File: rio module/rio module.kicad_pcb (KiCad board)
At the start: 2 copper layers, 60 x 45 mm, 11 parts, among them J1 MTJ-88ARX1-FSM-LG, J2 MTJ-88ARX1-FSM-LG, J3 Conn_01x02_Pin, J4 Conn_01x02_Pin, J5 Conn_01x02_Pin, J6 Conn_01x02_Pin, J7 Conn_01x02_Pin, SW1 SW_DPST

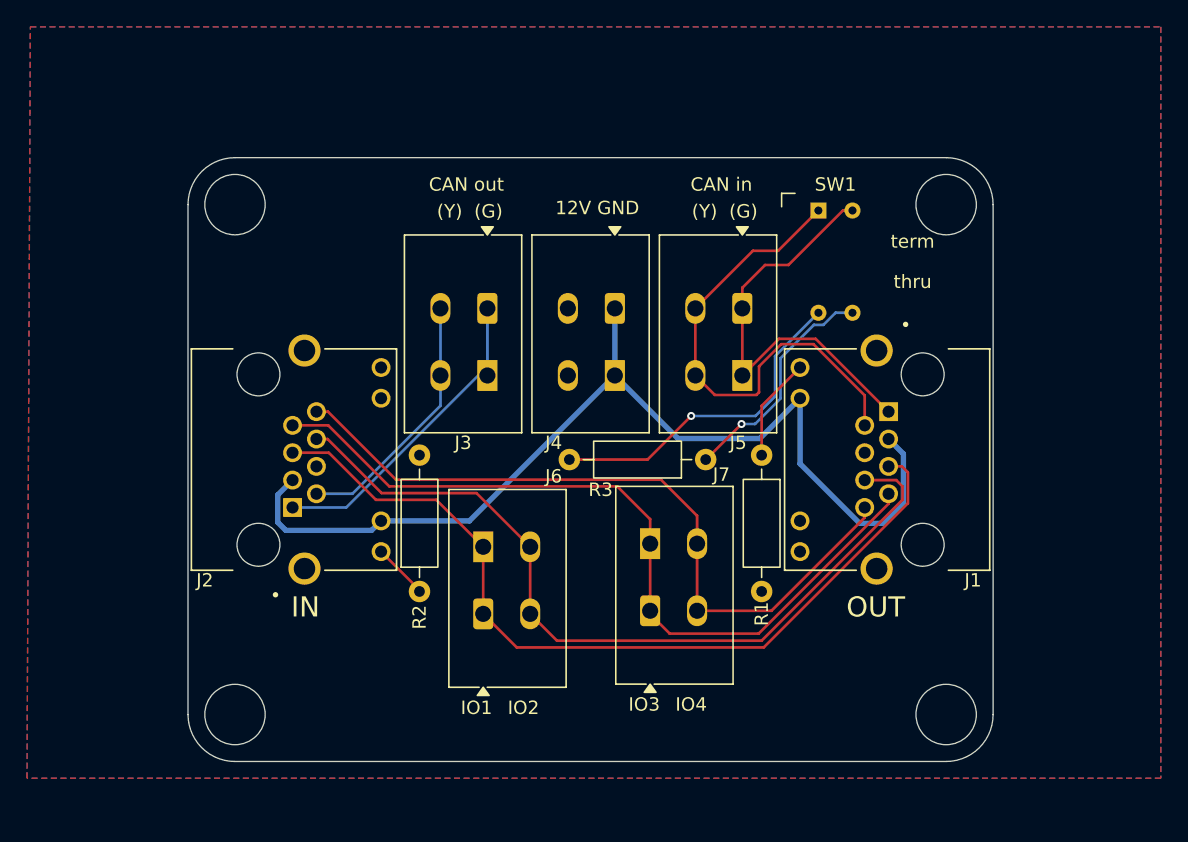
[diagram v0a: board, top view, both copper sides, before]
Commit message: removed mxp crossover, moved to hardwired DIO, switching from DIO WAGOs to Molex SL
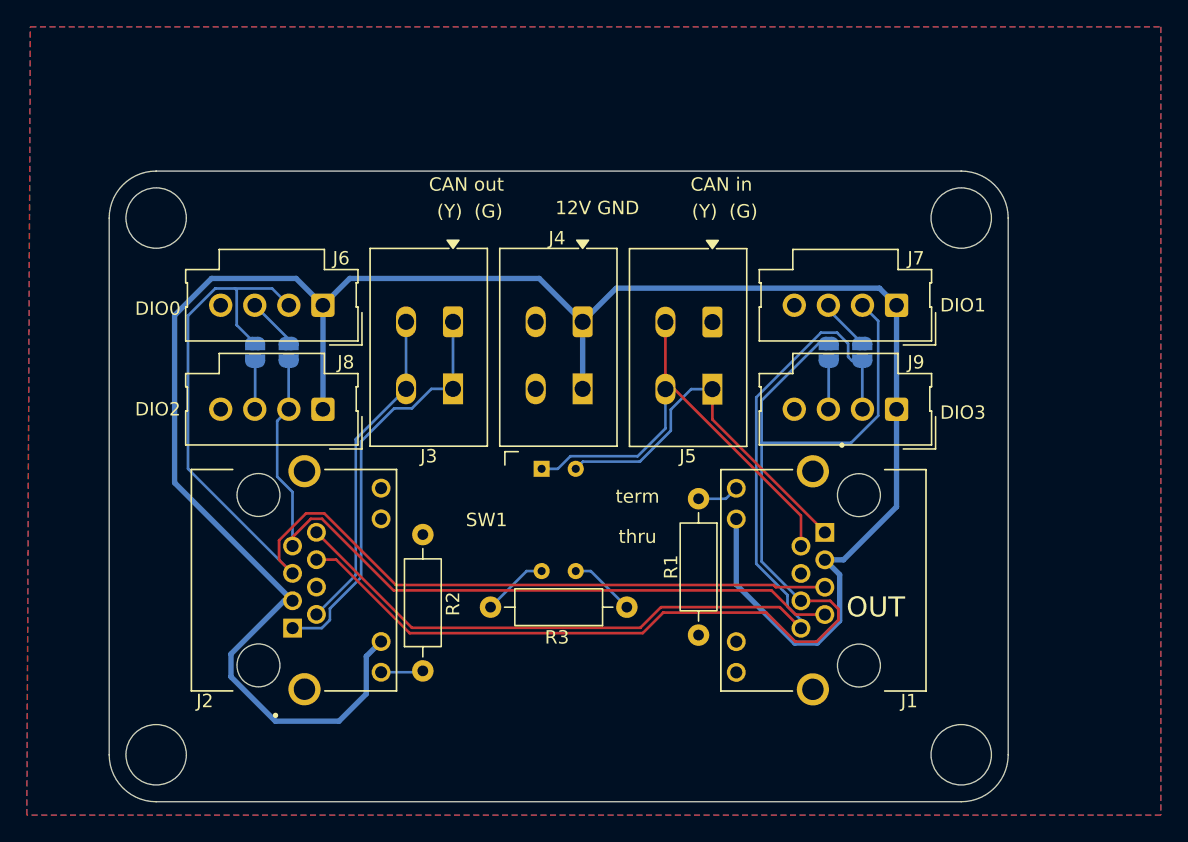
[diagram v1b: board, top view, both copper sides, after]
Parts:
- added J8: Conn_01x04_Pin, custom:Molex_SL_171971-0004_1x04_P2.54mm_Vertical, F.Cu at (55.6, 69.5)
- added J9: Conn_01x04_Pin, custom:Molex_SL_171971-0004_1x04_P2.54mm_Vertical, F.Cu at (98.3, 69.5)
- added REF**: SolderJumper-2_P1.3mm_Open_RoundedPad1.0x1.5mm, Jumper:SolderJumper-2_P1.3mm_Open_RoundedPad1.0x1.5mm, B.Cu at (95.8, 65.2)
- added REF**: SolderJumper-2_P1.3mm_Open_RoundedPad1.0x1.5mm, Jumper:SolderJumper-2_P1.3mm_Open_RoundedPad1.0x1.5mm, B.Cu at (93.2, 65.2)
- added REF**: SolderJumper-2_P1.3mm_Open_RoundedPad1.0x1.5mm, Jumper:SolderJumper-2_P1.3mm_Open_RoundedPad1.0x1.5mm, B.Cu at (53.0, 65.2)
- added REF**: SolderJumper-2_P1.3mm_Open_RoundedPad1.0x1.5mm, Jumper:SolderJumper-2_P1.3mm_Open_RoundedPad1.0x1.5mm, B.Cu at (50.5, 65.2)
- J6, J7: value Conn_01x02_Pin -> Conn_01x04_Pin; footprint custom:TerminalBlock_WAGO_2601-1102_1x02_P3.50mm_Horizontal w-model -> custom:Molex_SL_171971-0004_1x04_P2.54mm_Vertical
- moved J7 29.3 mm to (98.3, 61.8), turned to 180 degrees
- moved SW1 28.2 mm to (73.1, 77.8)
- moved J6 25.9 mm to (55.6, 61.8), turned to 180 degrees
- moved R3 12.5 mm to (78.2, 84.2)
- moved J1 10.2 mm to (95.5, 82.2)
- moved J2 8.99 mm to (50.8, 82.2)
- moved R2 5.93 mm to (63.0, 89.0)
- moved R1 5.72 mm to (83.5, 76.2)
- moved J3 2.75 mm to (65.2, 63.0)
- moved J4 2.60 mm to (74.9, 63.0)
- moved J5 2.45 mm to (84.6, 63.0)
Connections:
- J1 pad 5: /IO1 -> /DIO 0
- J1 pad 6: /IO2 -> /DIO 1
- J1 pad 7: /IO3 -> /DIO 2
- J1 pad 8: /IO4 -> /DIO 3
- J2 pad 5: /IO1 -> /DIO 0
- J2 pad 6: /IO2 -> /DIO 1
- J2 pad 7: /IO3 -> /DIO 2
- J2 pad 8: /IO4 -> /DIO 3
- J6 pad 1: /IO1 -> /12V
- J6 pad 2: /IO2 -> /DIO 0
- J7 pad 1: /IO3 -> /12V
- J7 pad 2: /IO4 -> /DIO 1
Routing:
- net /DIO 1: track 0.00 -> 88.4 mm
- net /12V: track 76.0 -> 163.9 mm
- net /DIO 0: track 0.00 -> 82.7 mm
- net /DIO 3: track 0.00 -> 73.9 mm
- net /IO1: track 63.2 -> 0.00 mm
- net /IO2: track 61.2 -> 0.00 mm
- net /IO3: track 59.7 -> 0.00 mm
- net /DIO 2: track 0.00 -> 58.5 mm
- net /IO4: track 55.0 -> 0.00 mm
- net Net-(R3-Pad2): track 24.8 -> 4.92 mm, vias 1 -> 0
- net Net-(R3-Pad1): track 17.2 -> 4.92 mm, vias 1 -> 0
- net Net-(J3-Pin_1): track 23.6 -> 30.8 mm
- net Net-(J3-Pin_2): track 19.2 -> 24.6 mm
- net Net-(J1-Pad9): track 7.71 -> 3.14 mm
- net DIO3_C: track 0.00 -> 3.90 mm
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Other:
- board size 60 x 45 mm -> 67 x 47 mm
- board text added: "DIO 0 alt"
- board text added: "DIO 1 alt"
- board text added: "DIO 2 alt"
- board text added: "DIO 3 alt"
- board text added: "DIO0"
- board text added: "DIO1"
- board text added: "DIO2"
- board text added: "DIO3"
- board text removed: "IN"
- board text removed: "IO1"
- board text removed: "IO2"
- board text removed: "IO3"
- board text removed: "IO4"

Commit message: final major changes, exported for JLCPCB
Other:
- board text added: "IN"
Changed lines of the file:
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@@
 		(tenting front back)
 		(pcbplotparams
-			(layerselection 0x00000000_00000000_55555555_5755f5ff)
+			(layerselection 0x00000000_00000000_55555555_575555ff)
 			(plot_on_all_layers_selection 0x00000000_00000000_00000000_00000000)
 			(disableapertmacros no)
-			(usegerberextensions no)
-			(usegerberattributes yes)
-			(usegerberadvancedattributes yes)
+			(usegerberextensions yes)
+			(usegerberattributes no)
+			(usegerberadvancedattributes no)
 			(creategerberjobfile yes)
 			(dashed_line_dash_ratio 12.000000)
@@
 			(plotframeref no)
 			(mode 1)
-			(useauxorigin no)
+			(useauxorigin yes)
 			(hpglpennumber 1)
 			(hpglpenspeed 20)
@@
 			(plotpadnumbers no)
 			(hidednponfab no)
-			(sketchdnponfab yes)
-			(crossoutdnponfab yes)
-			(subtractmaskfromsilk no)
+			(sketchdnponfab no)
+			(crossoutdnponfab no)
+			(subtractmaskfromsilk yes)
 			(outputformat 1)
 			(mirror no)
-			(drillshape 1)
+			(drillshape 0)
 			(scaleselection 1)
-			(outputdirectory "")
+			(outputdirectory "JLC/")
 		)
 	)
@@
 		(tags "THT Terminal Block WAGO 2601-1102 pitch 3.5mm size 8.5x14.5mm drill 1.2mm pad 2.3mm")
 		(property "Reference" "J4"
-			(at 1.91 6.2325 0)
+			(at 6.66 -10.0175 0)
 			(layer "F.SilkS")
 			(effects
@@
 	)
 	(gr_text "(Y)  (G)"
-		(at 85.5 54.75 0)
+		(at 82.75 55.75 0)
 		(layer "F.SilkS")
 		(effects
@@
 	)
 	(gr_text "OUT\n"
-		(at 96.75 84.25 0)
+		(at 95.75 92.25 0)
 		(layer "F.SilkS")
 		(effects
@@
 	)
 	(gr_text "CAN in\n"
-		(at 85.25 52.75 0)
+		(at 82.5 53.75 0)
 		(layer "F.SilkS")
 		(effects
@@
 	)
 	(gr_text "CAN out"
-		(at 66.25 52.75 0)
+		(at 63.25 53.75 0)
 		(layer "F.SilkS")
 		(effects
@@
 	)
 	(gr_text "(Y)  (G)"
-		(at 66.5 54.75 0)
+		(at 63.5 55.75 0)
 		(layer "F.SilkS")
 		(effects
@@
 		)
 	)
+	(gr_text "IN"
+		(at 57 92.25 0)
+		(layer "F.SilkS")
+		(effects
+			(font
+				(size 1.5 1.5)
+				(thickness 0.15)
+			)
+		)
+	)
 	(gr_text "12V GND"
-		(at 76 54.5 0)
+		(at 73.25 55.5 0)
 		(layer "F.SilkS")
 		(effects
